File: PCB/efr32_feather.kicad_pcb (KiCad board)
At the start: 2 copper layers, 50.8 x 22.9 mm, 39 parts, among them J1 Feather_1, J2 USB, J3 Battery, J4 Feather_2, J5 DEBUG, Q1 DMG2301L, SW1 RESET, U1 TPD2EUSB30, U2 AP2112K-3.3, U3 CP2102N-A01-GQFN24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

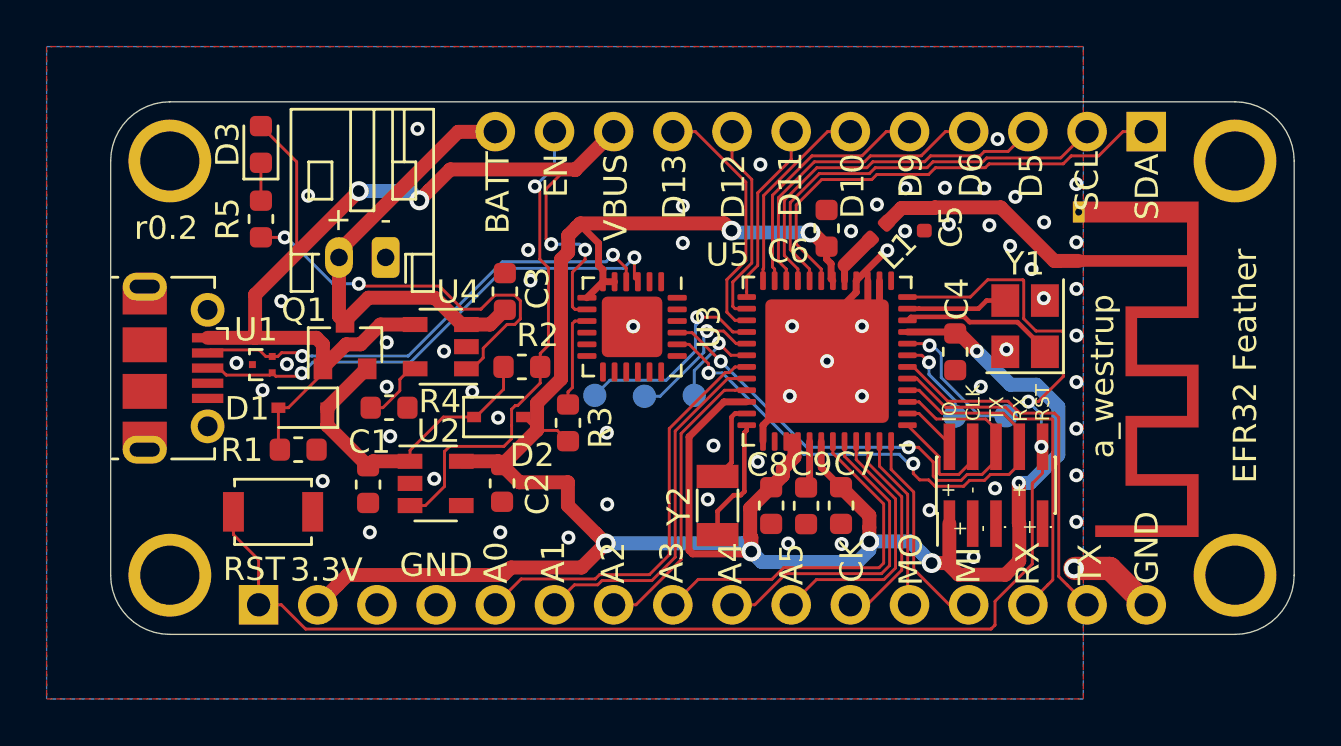
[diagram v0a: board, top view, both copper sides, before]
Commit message: Change debug connector
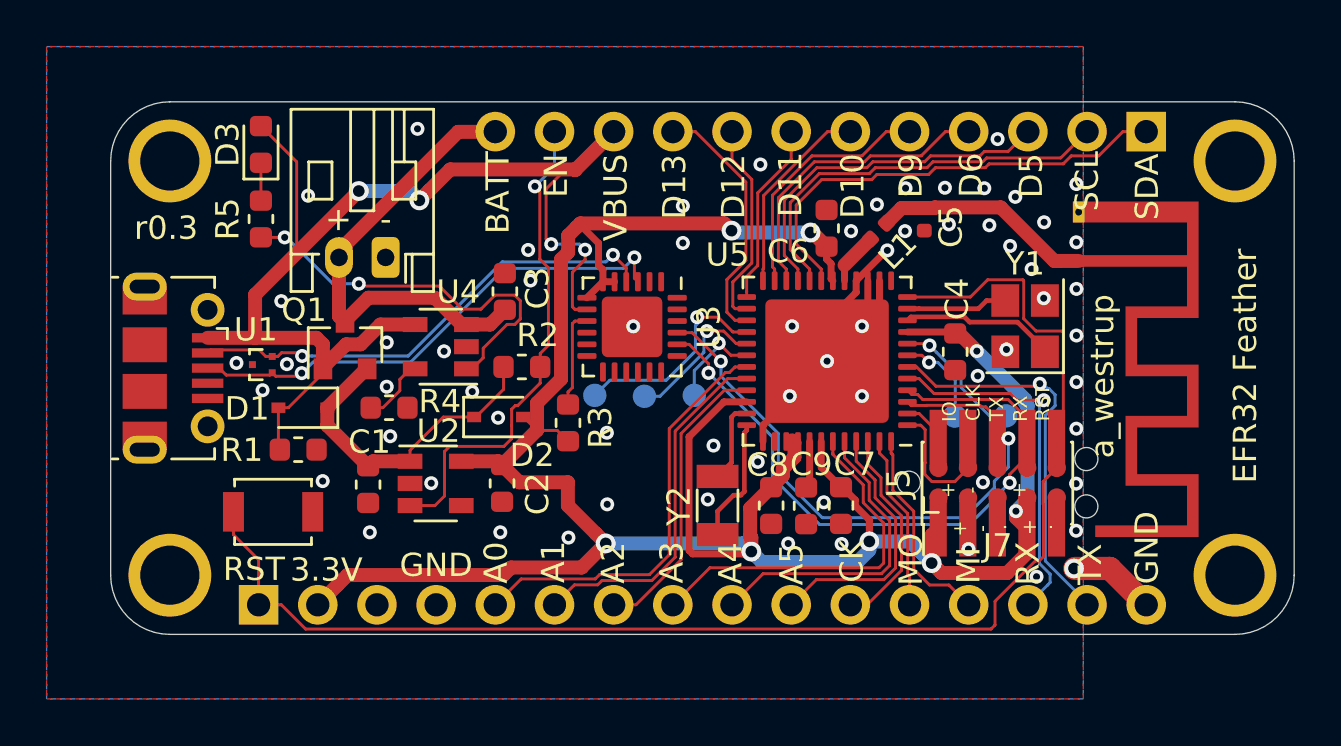
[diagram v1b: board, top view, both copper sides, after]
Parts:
- added J7: TagConnect, Connector:Tag-Connect_TC2050-IDC-NL_2x05_P1.27mm_Vertical, F.Cu at (184.8, 144.7)
- J5: footprint Connector_PinHeader_1.00mm:PinHeader_2x05_P1.00mm_Vertical_SMD -> Connector_PinHeader_1.27mm:PinHeader_2x05_P1.27mm_Vertical_SMD
- moved J5 0.10 mm to (184.8, 144.7)
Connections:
- J5 pad 5: Net-(J5-Pad5) -> /NC1
- J5 pad 9: Net-(J5-Pad9) -> /NC2
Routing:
- net /USB_TX: track 22.6 -> 28.0 mm
- net /USB_RX: track 25.1 -> 29.5 mm
- net /SWDCLK: track 4.94 -> 6.30 mm
- net GND: track 22.7 -> 24.0 mm, vias 64 -> 65
- net /NC2: track 0.00 -> 1.34 mm
- net /NC1: track 0.00 -> 1.34 mm
- net /D1_TX: track 15.9 -> 16.9 mm, vias 0 -> 1
- net +3V3: track 111.0 -> 111.9 mm
- net /SWDIO: track 2.46 -> 3.18 mm
- net /NRESET: track 60.0 -> 59.3 mm, vias 2 -> 0
- net /D0_RX: track 15.4 -> 15.7 mm, vias 0 -> 1
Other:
- board text added: "r0.3"
- board text removed: "r0.2"
